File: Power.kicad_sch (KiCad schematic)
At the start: 51 parts, among them IC4 TPS65251-1RHAR, U10 TPS62420DRCTG4

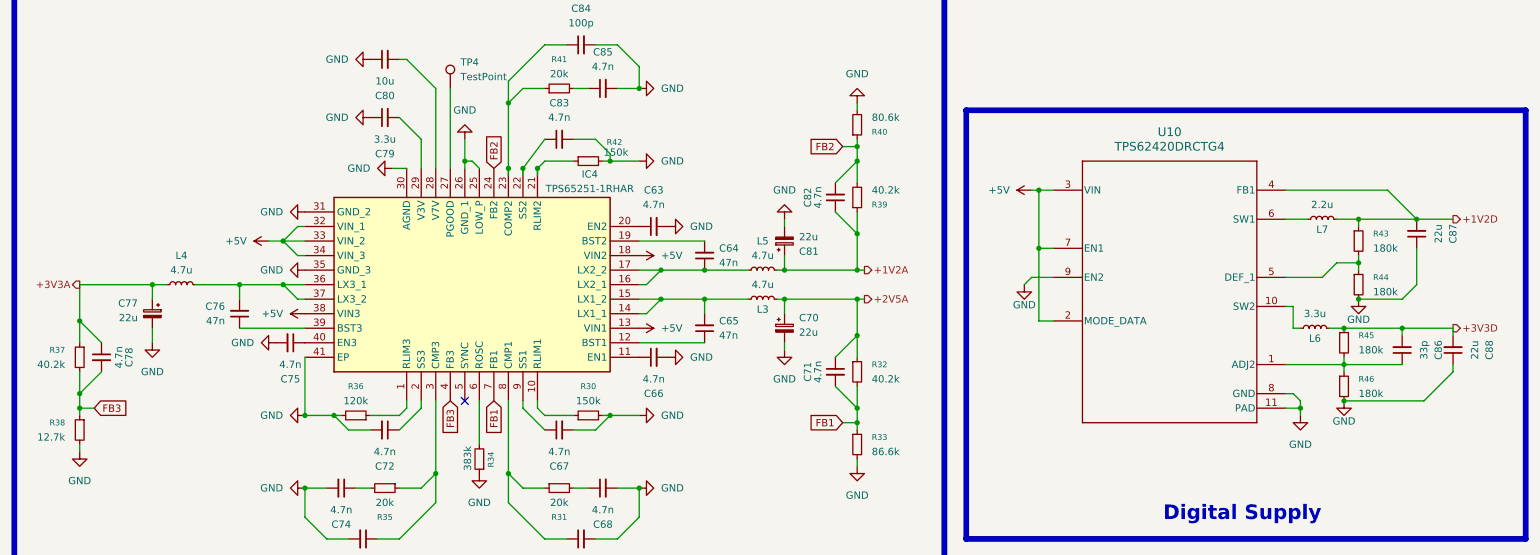
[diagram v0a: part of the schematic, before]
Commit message: Digital Reg Changed
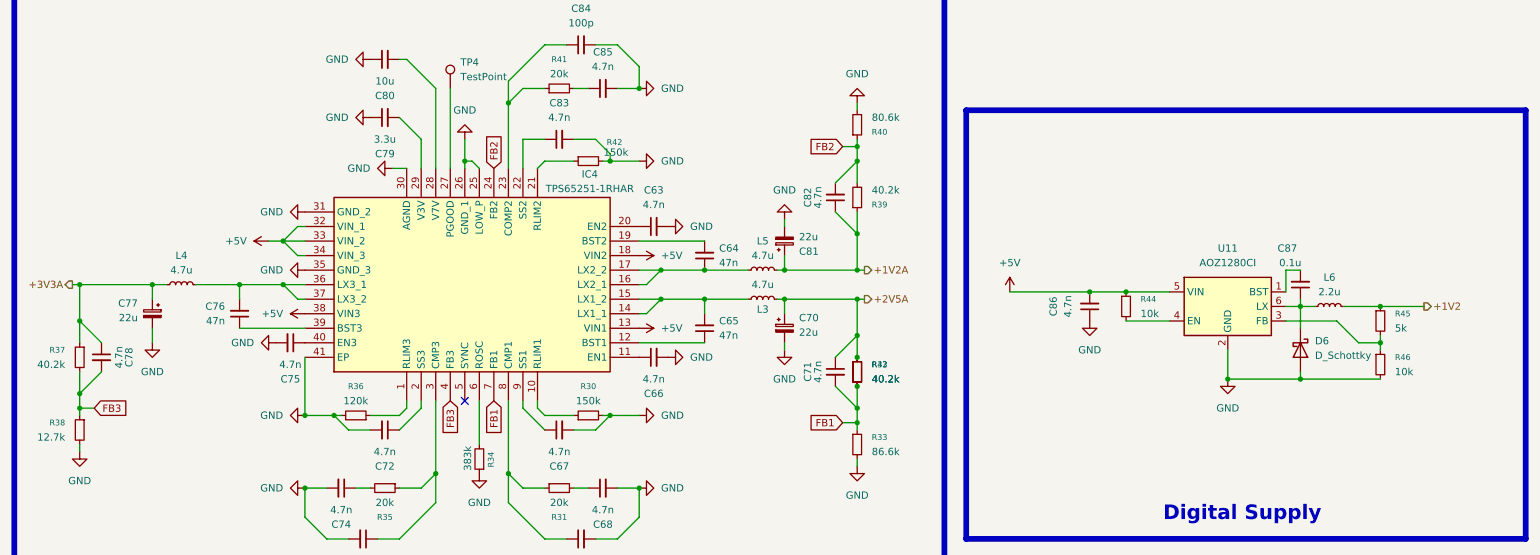
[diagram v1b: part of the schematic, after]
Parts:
- removed C88: 22u, symbol Device:C_Small
- removed L7: 2.2u, symbol Device:L_Small
- removed U10: TPS62420DRCTG4, DRC0010J, symbol TPS62420DRCTG4:TPS62420DRCTG4
- added D6: D_Schottky, symbol Device:D_Schottky
- added U11: AOZ1280CI, Package_TO_SOT_SMD:SOT-23-6, symbol Regulator_Switching:AOZ1280CI
- C86: value 33p -> 4.7n
- C87: value 22u -> 0.1u
- L6: value 3.3u -> 2.2u
- R43: value 180k -> 40.2k
- R44, R46: value 180k -> 10k
- R45: value 180k -> 5k
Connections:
- net +2V5A: now also R43.1
- net +5V: now also C86.2, R44.1, U11.5 (VIN)
- net FB1: now also R43.2
- net GND: now also C86.1, D6.2 (A), U11.2 (GND); no longer C87.1, R44.2
- net at R45.2, R46.1: now also U11.3 (FB); no longer C86.1
- net at L6.1: now also C87.1, D6.1 (K), U11.6 (LX)
- net +1V2D: no longer names the net of C87.2
- net +1V2D: now also U11.1 (BST); no longer R43.1
- net +3V3D renamed +1V2
- net +1V2: no longer C86.2
- new net: R44.2, U11.4 (EN)

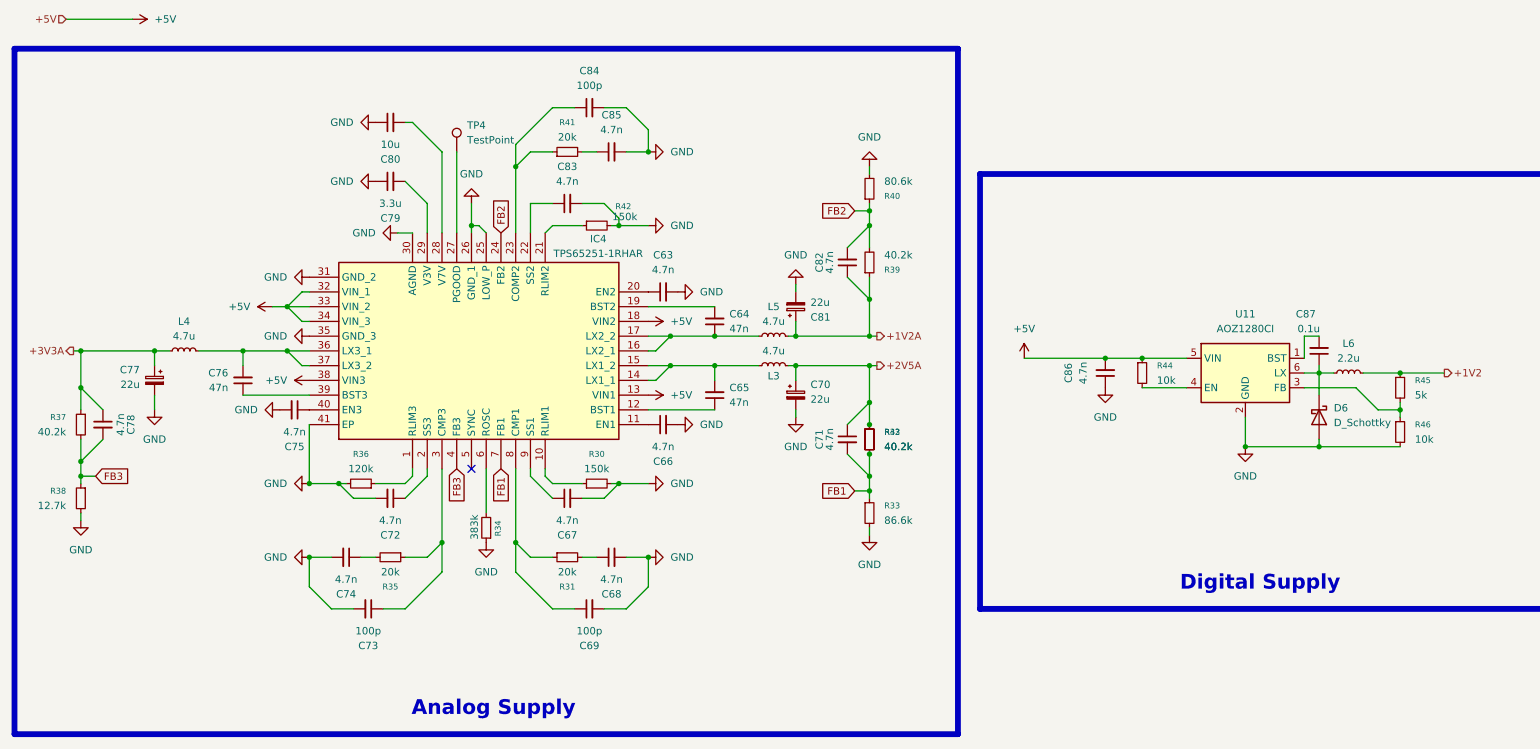
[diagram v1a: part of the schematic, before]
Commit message: Sheet name edit and changed to net labels
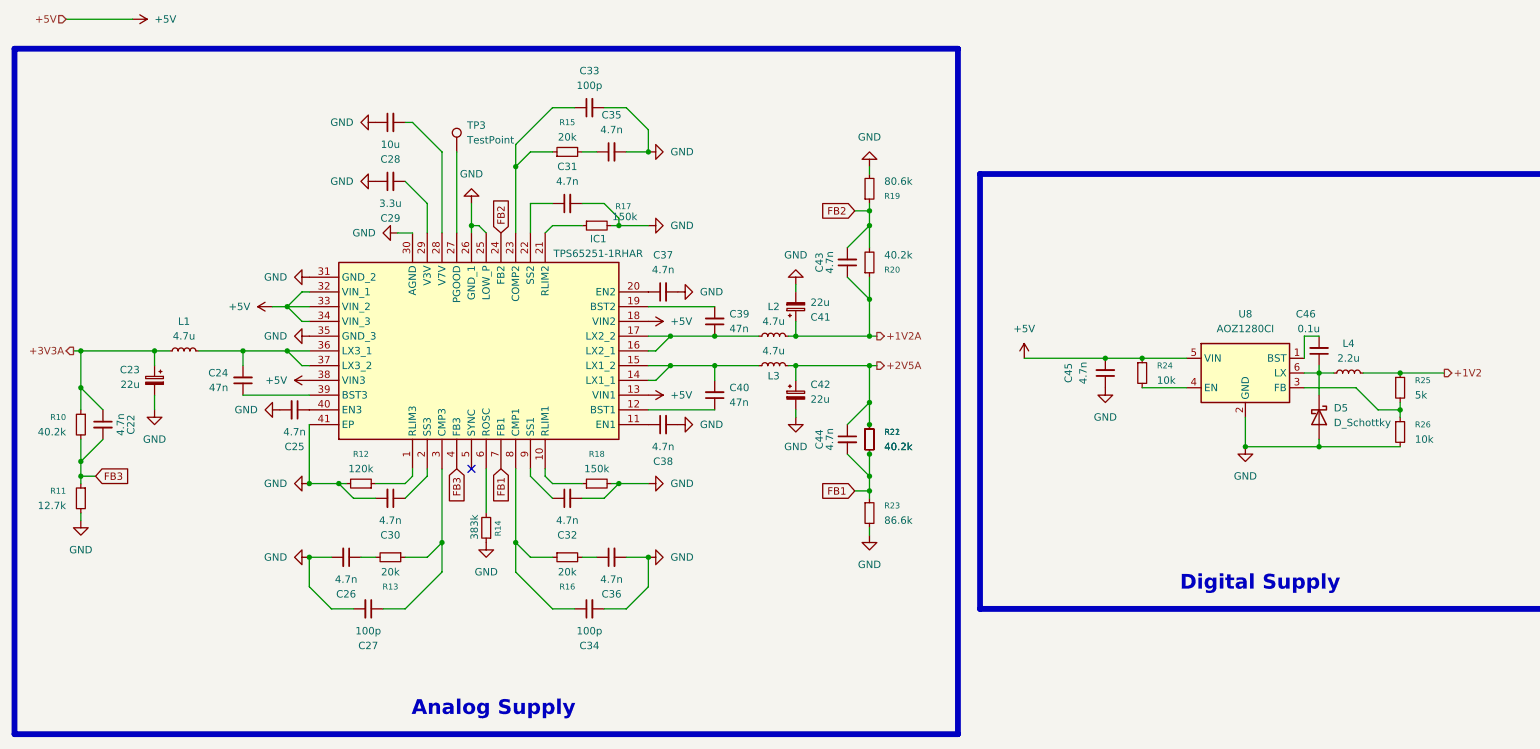
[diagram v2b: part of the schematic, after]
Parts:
- renumbered C78 to C22, C77 to C23, C76 to C24, C75 to C25, C74 to C26, C73 to C27, C80 to C28, C79 to C29, C72 to C30, C83 to C31, C67 to C32, C84 to C33, C69 to C34, C85 to C35, C68 to C36, C63 to C37, C66 to C38, C64 to C39, C65 to C40, C81 to C41, C70 to C42, C82 to C43, C71 to C44, C86 to C45, C87 to C46, D6 to D5, IC4 to IC1, L4 to L1, L5 to L2, L6 to L4, R37 to R10, R38 to R11, R36 to R12, R35 to R13, R34 to R14, R41 to R15, R31 to R16, R42 to R17, R30 to R18, R40 to R19, R39 to R20, R43 to R21, R32 to R22, R33 to R23, R44 to R24, R45 to R25, R46 to R26, TP4 to TP3, U11 to U8

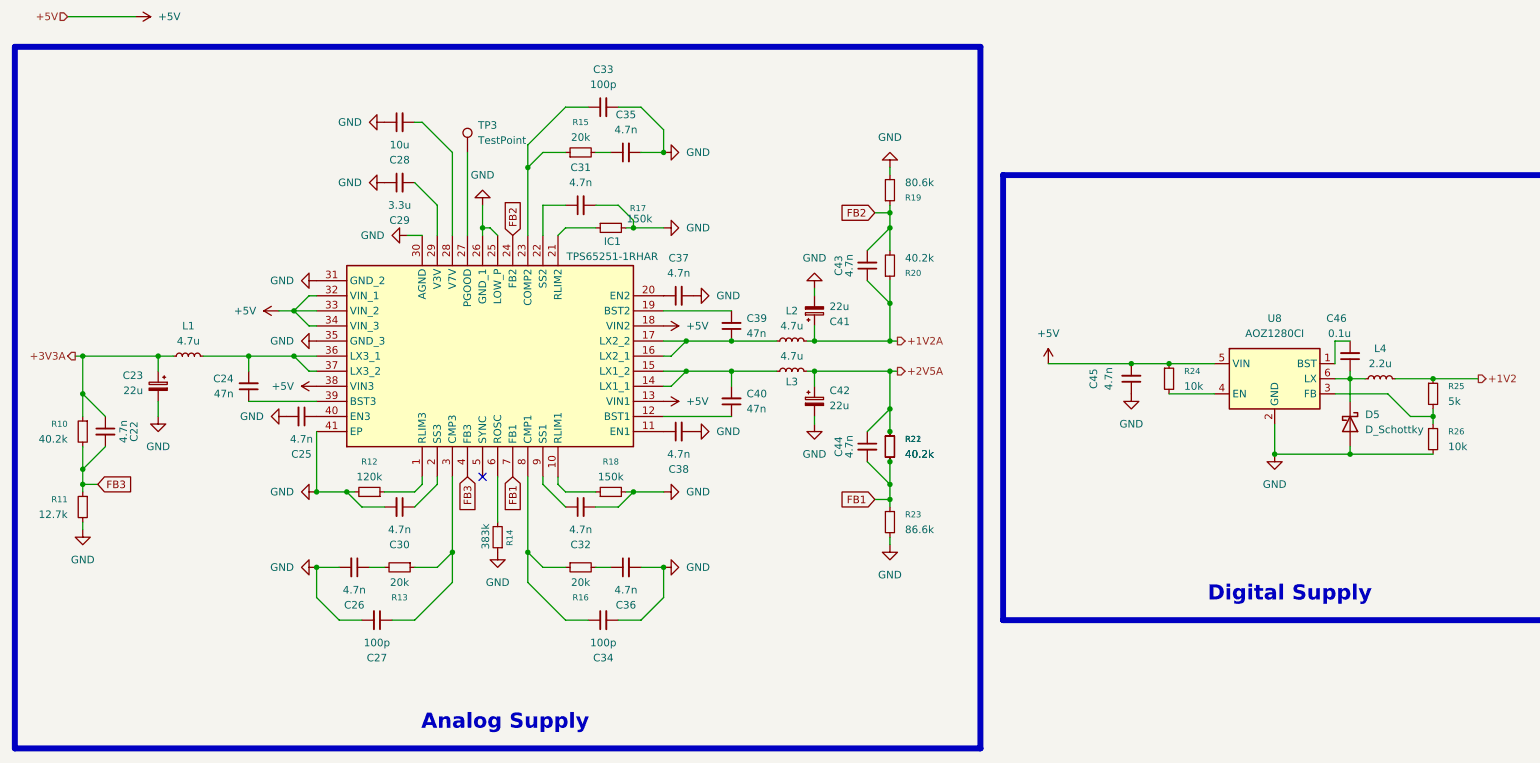
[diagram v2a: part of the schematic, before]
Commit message: Started Ethernet design
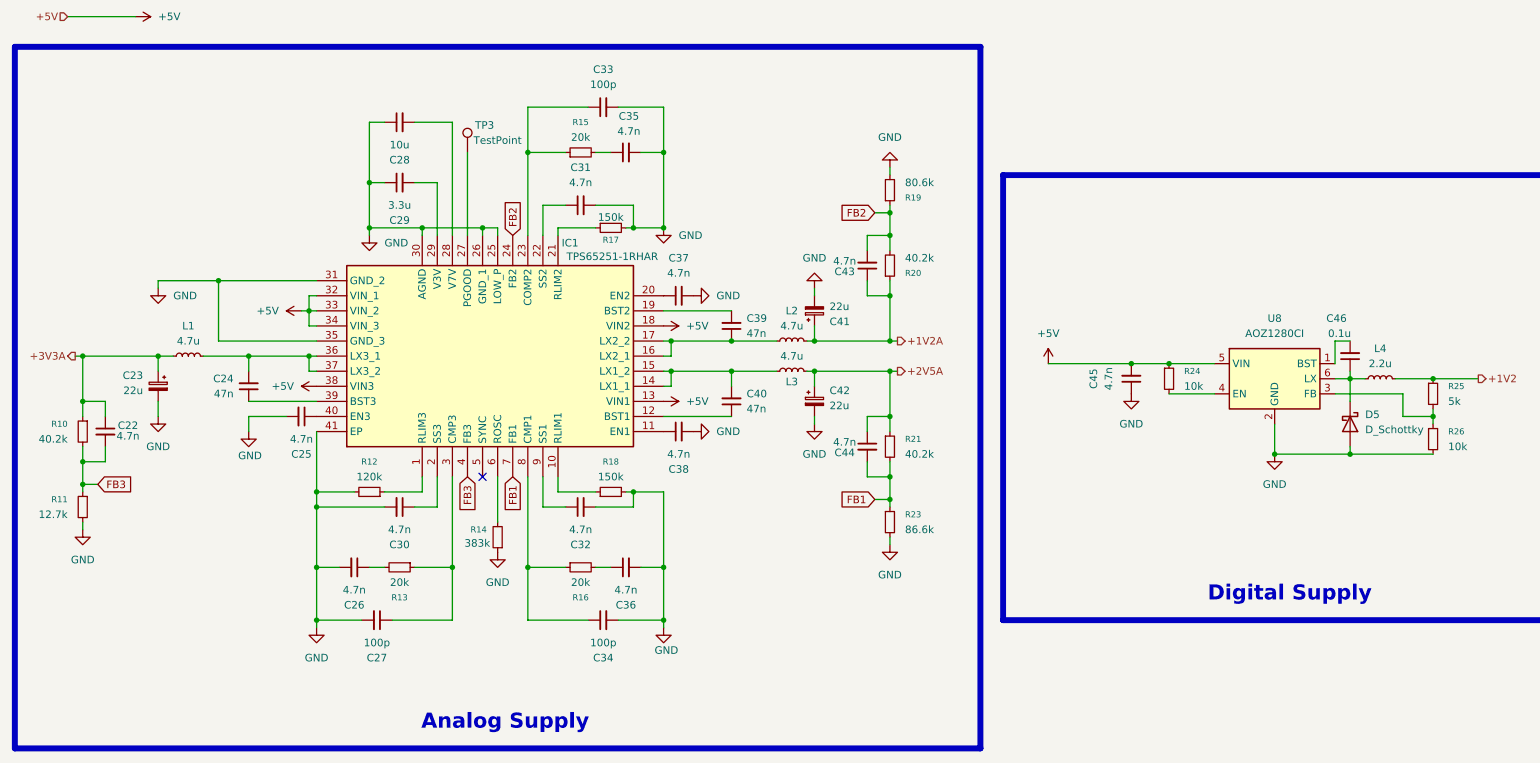
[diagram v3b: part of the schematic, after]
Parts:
- removed R22: 40.2k, symbol Device:R_Small

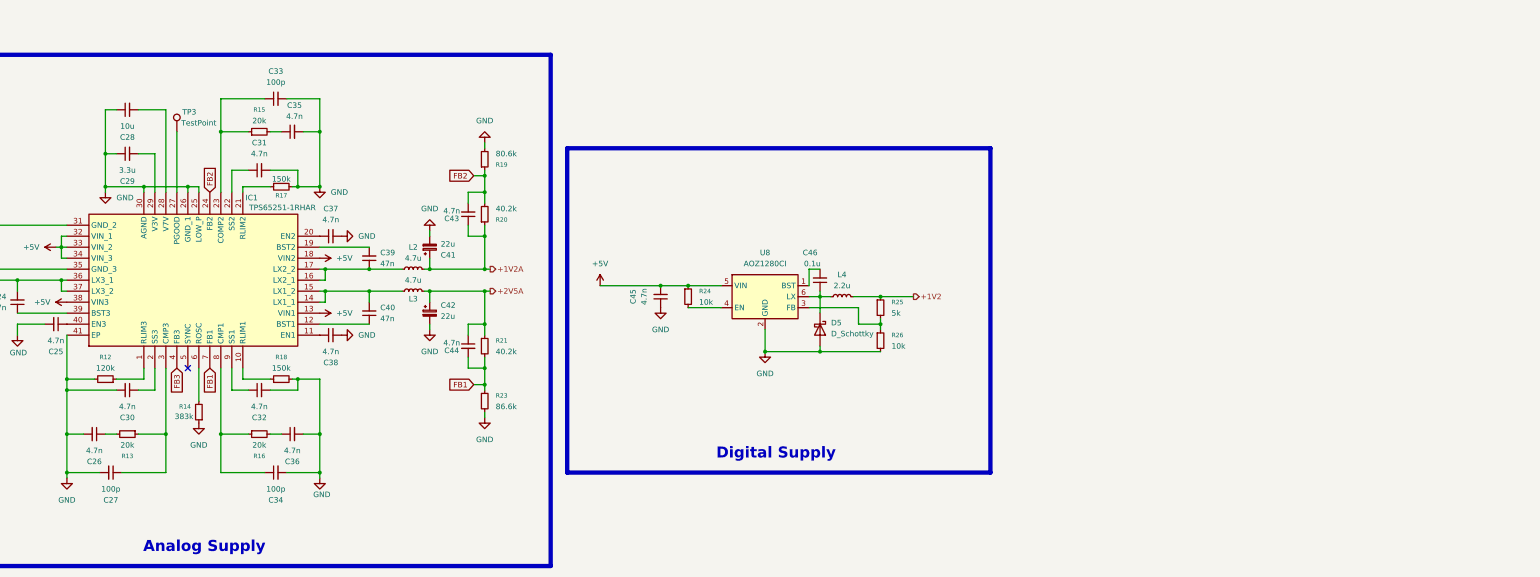
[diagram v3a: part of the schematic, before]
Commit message: Buck converter output voltage changed
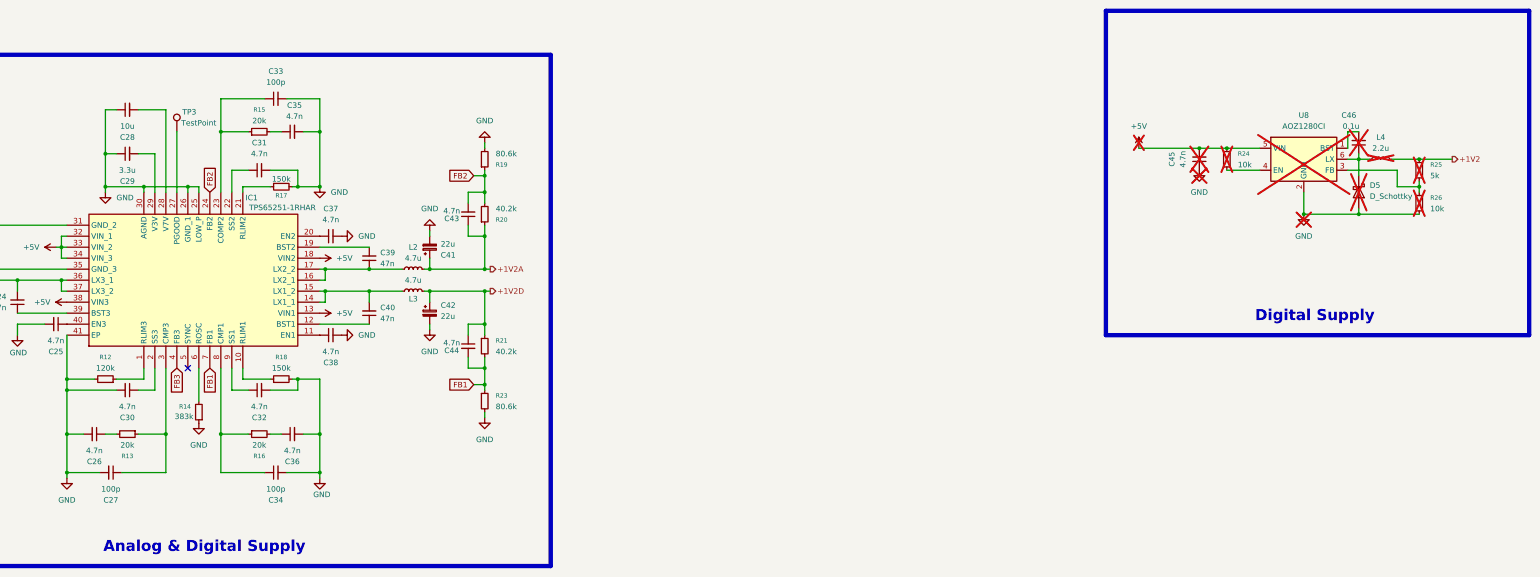
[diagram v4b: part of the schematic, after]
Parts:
- C45, C46, D5, L4, R24, R25, R26, U8: now not fitted; now left out of the parts list
- R23: value 86.6k -> 80.6k
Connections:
- net +2V5A renamed +1V2D

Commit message: Swiitched to JSM561
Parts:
- removed C45: 4.7n, symbol Device:C_Small
- removed C46: 0.1u, symbol Device:C_Small
- removed D5: D_Schottky, symbol Device:D_Schottky
- removed L4: 2.2u, symbol Device:L_Small
- removed R24, R26: 10k, symbol Device:R_Small
- removed R25: 5k, symbol Device:R_Small
- removed U8: AOZ1280CI, Package_TO_SOT_SMD:SOT-23-6, symbol Regulator_Switching:AOZ1280CI
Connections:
- removed net GND: C23.2, C25.2, C26.2, C27.2, C28.1, C29.1, C30.2, C31.2, C32.2, C33.2, C34.2, C35.2, C36.2, C37.2, C38.2, C41.2, C42.2, IC1.25 (LOW_P), IC1.26 (GND_1), IC1.30 (AGND), IC1.31 (GND_2), IC1.35 (GND_3), IC1.41 (EP), R11.2, R12.2, R14.1, R17.2, R18.2, R19.2, R23.2
- new net: C26.2, C27.2, C30.2, IC1.41 (EP), R12.2
- new net: C31.2, C33.2, C35.2, R17.2
- new net: C28.1, C29.1, IC1.25 (LOW_P), IC1.26 (GND_1), IC1.30 (AGND)
- new net: IC1.31 (GND_2), IC1.35 (GND_3)
- new net: C32.2, C34.2, C36.2, R18.2
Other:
- moved on the sheet: C22, C23, C24, C25, C26, C27, C28, C29, C30, C31, C32, C33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
